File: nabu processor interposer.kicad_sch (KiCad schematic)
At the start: 4 parts, among them J1 5V EXTRA, U1 LP3963-3.3

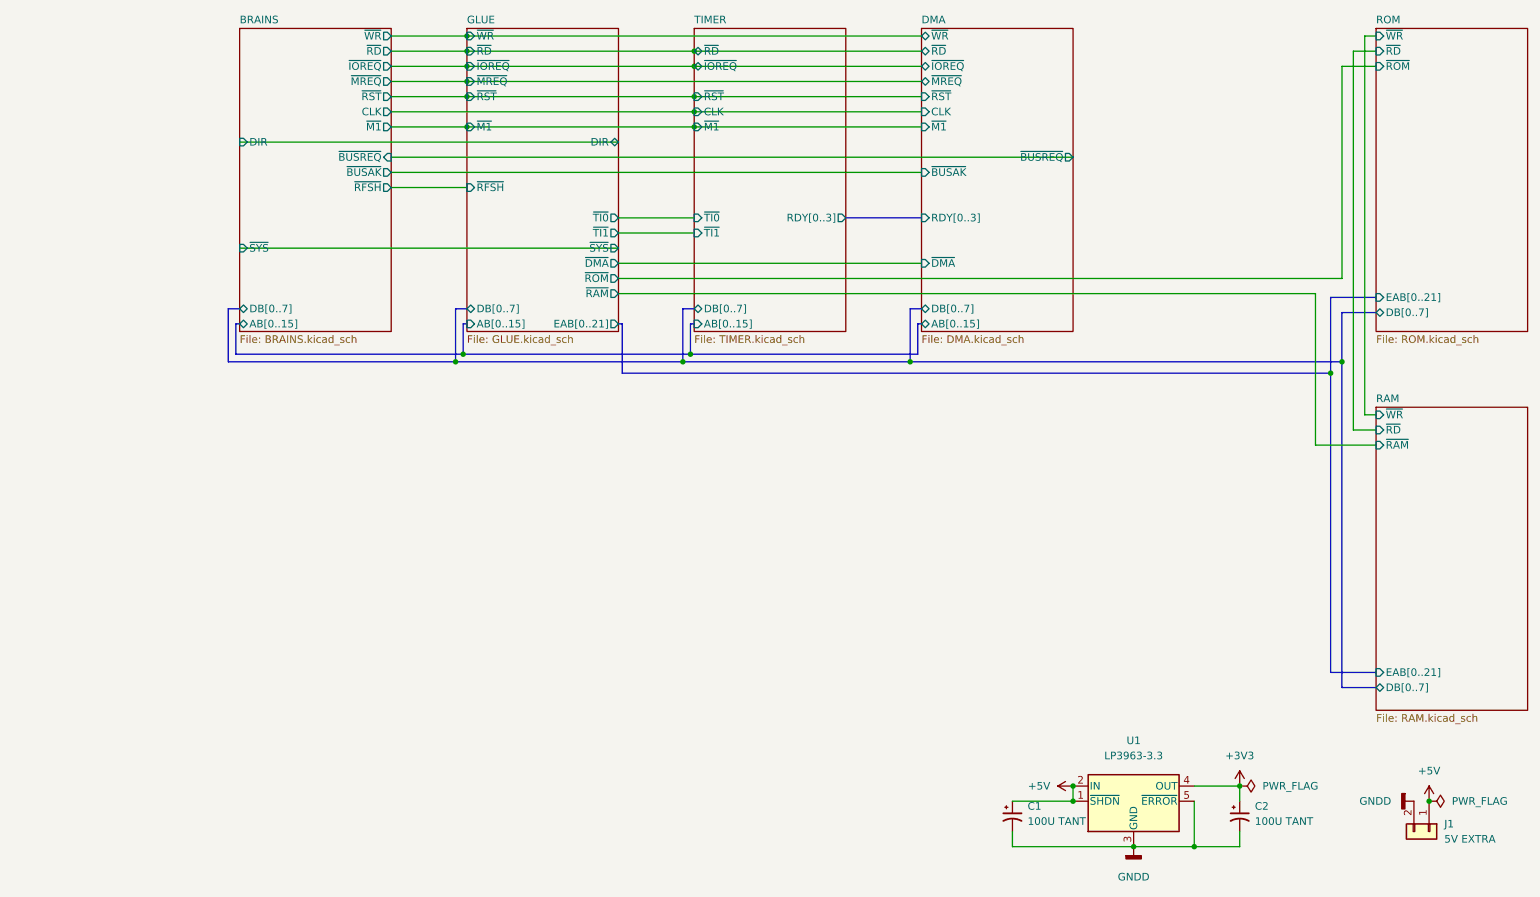
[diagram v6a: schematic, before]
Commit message: final hardware revision
final update to the hardware:
- removed flash
- added battery backup switch-over
- increased ram to 4MB
- added ramboot/netboot option by using reads to write-only ports to trigger/toggle
- fixed a logic bug i should have caught in writes to the mapper registers (using bits 14&15 instead of 1&0)
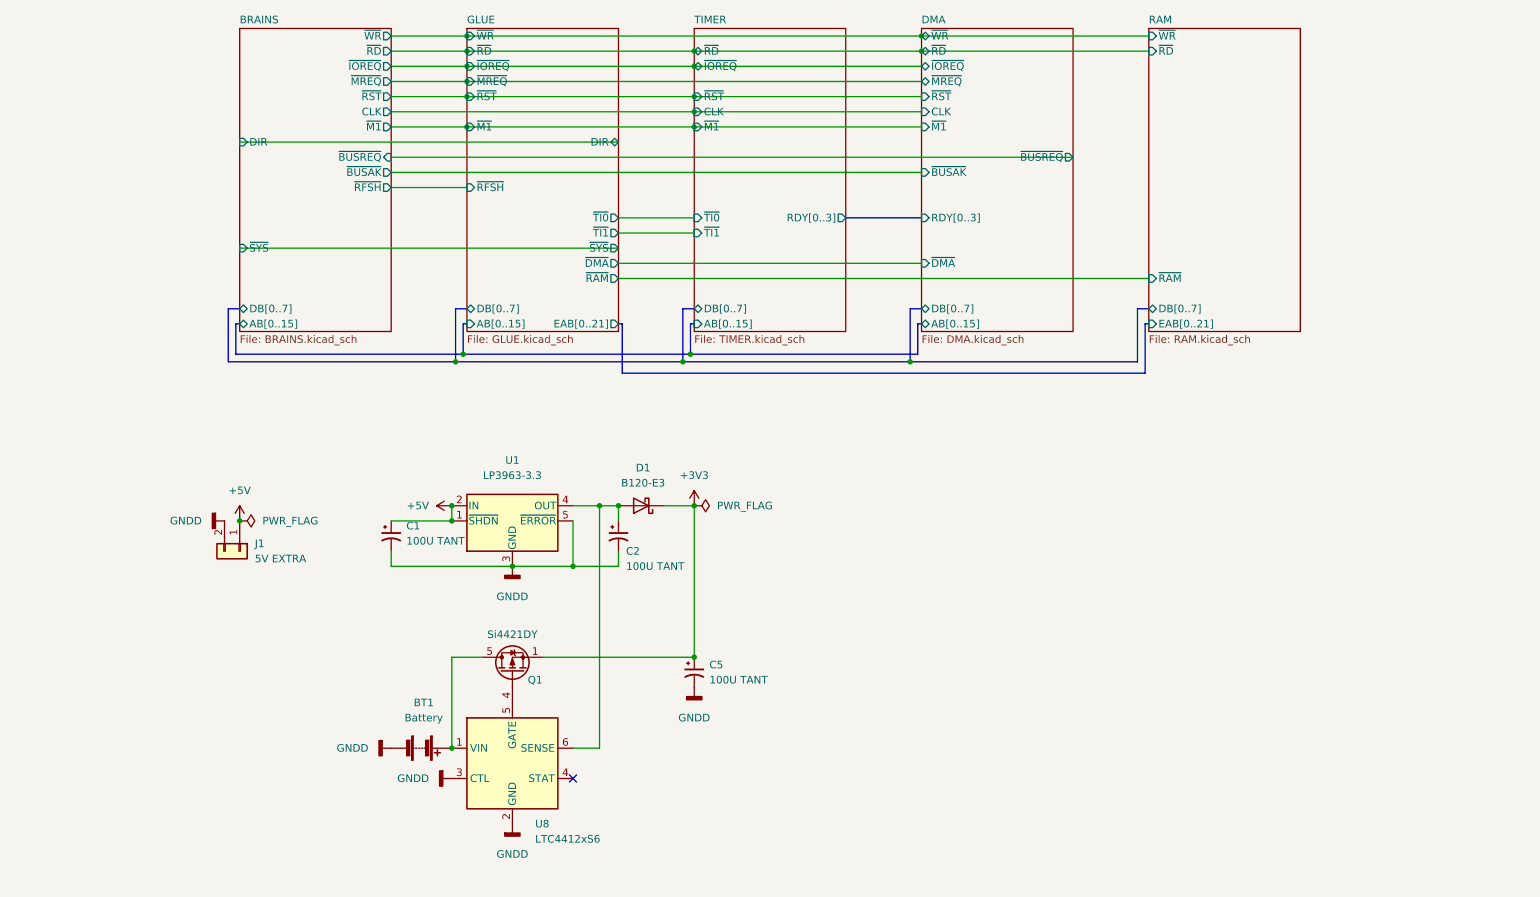
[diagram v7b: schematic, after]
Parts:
- added BT1: Battery, Battery:BatteryHolder_Keystone_2462_2xAA, symbol Device:Battery
- added C5: 100U TANT, Capacitor_Tantalum_SMD:CP_EIA-3528-15_AVX-H, symbol Device:C_Polarized_Small_US
- added D1: B120-E3, Diode_SMD:D_SMA, symbol Diode:B120-E3
- added Q1: Si4421DY, Package_SO:SO-8_3.9x4.9mm_P1.27mm, symbol Device:Q_PMOS_SGD
- added U8: LTC4412xS6, Package_TO_SOT_SMD:TSOT-23-6, symbol Power_Management:LTC4412xS6
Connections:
- net +3V3: now also C5.1, D1.1 (K), Q1.1 (S), Q1.2, Q1.3; no longer C2.1, U1.4 (OUT)
- net GNDD: now also BT1.2 (-), C5.2, U8.2 (GND), U8.3 (CTL)
- new net: C2.1, D1.2 (A), U1.4 (OUT), U8.6 (SENSE)
- new net: BT1.1 (+), Q1.5 (D), Q1.6, Q1.7, Q1.8, U8.1 (VIN)
- new net: Q1.4 (G), U8.5 (GATE)
- no-connect marks 0 -> 1
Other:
- removed sheet ROM
- sheet GLUE ports: added none; removed ~{ROM}
- moved on the sheet: C1, C2, J1, U1
